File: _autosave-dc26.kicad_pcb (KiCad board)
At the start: 4 copper layers, 129.2 x 142.3 mm, 709 parts, among them J1 CONN_01X10, J2 CONN_01X10, J3 CONN_01X10, Y1 Crystal

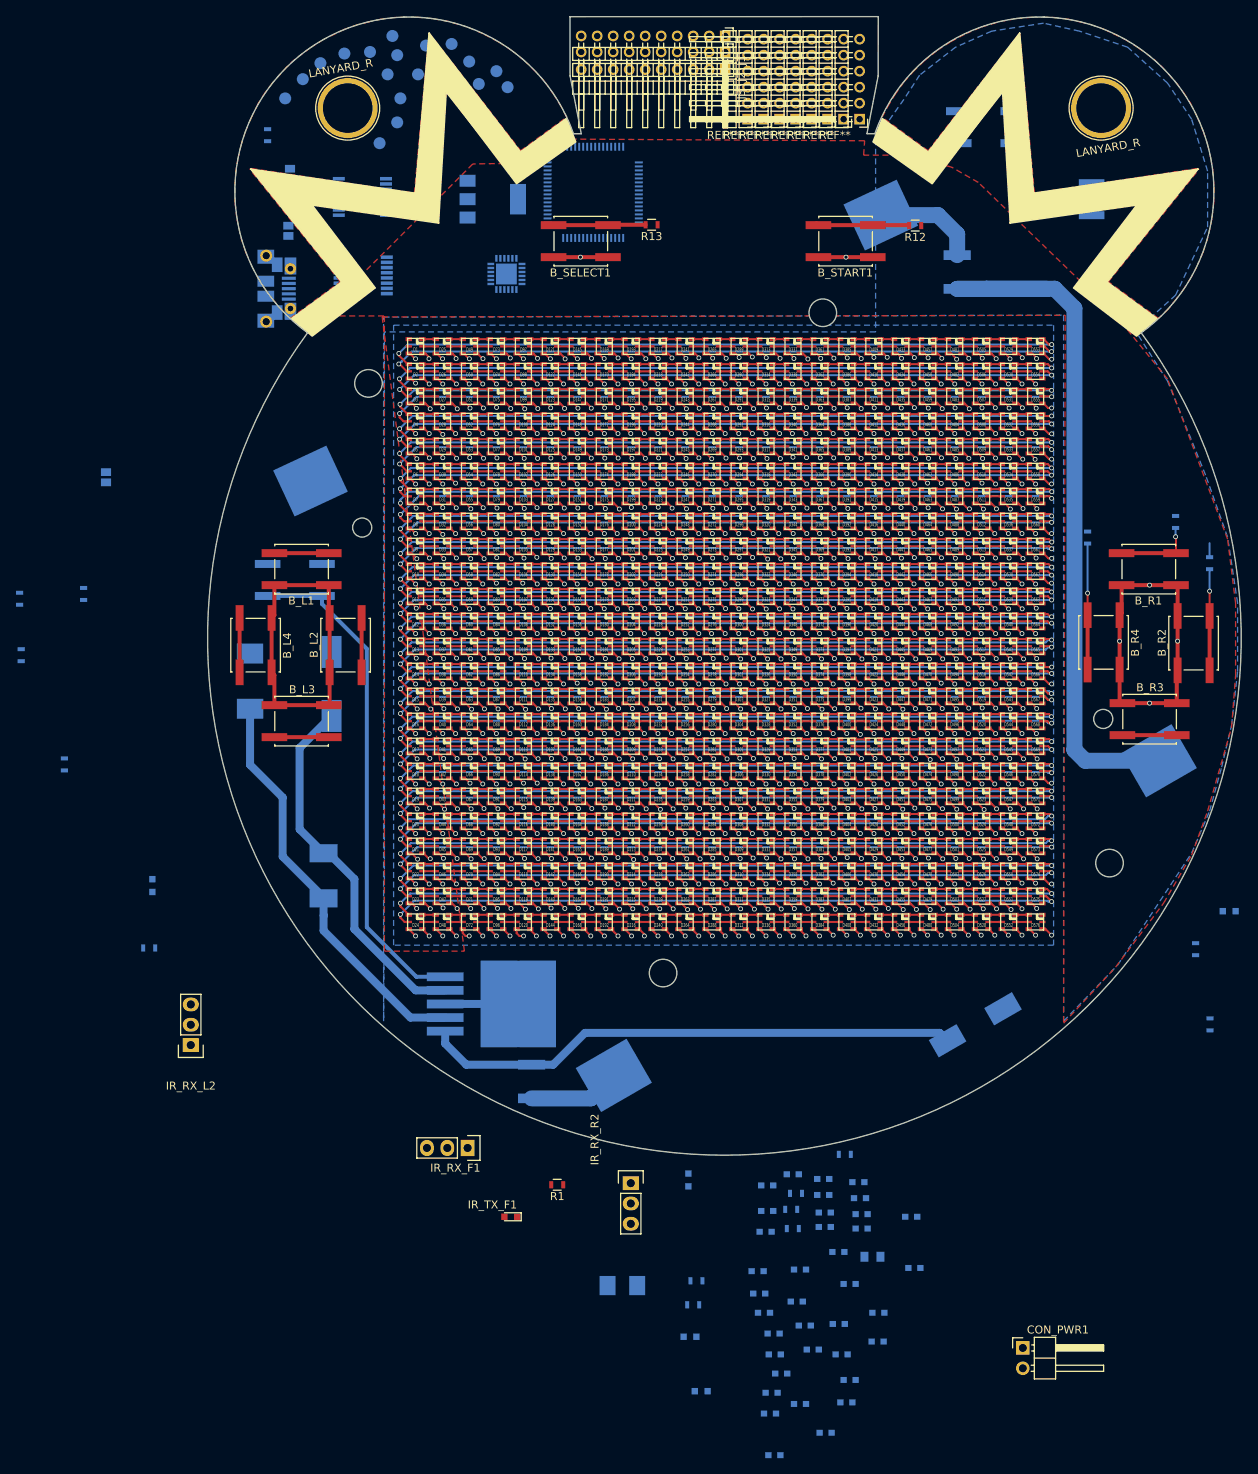
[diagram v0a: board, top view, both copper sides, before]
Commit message: zone movement + routing of all circuits
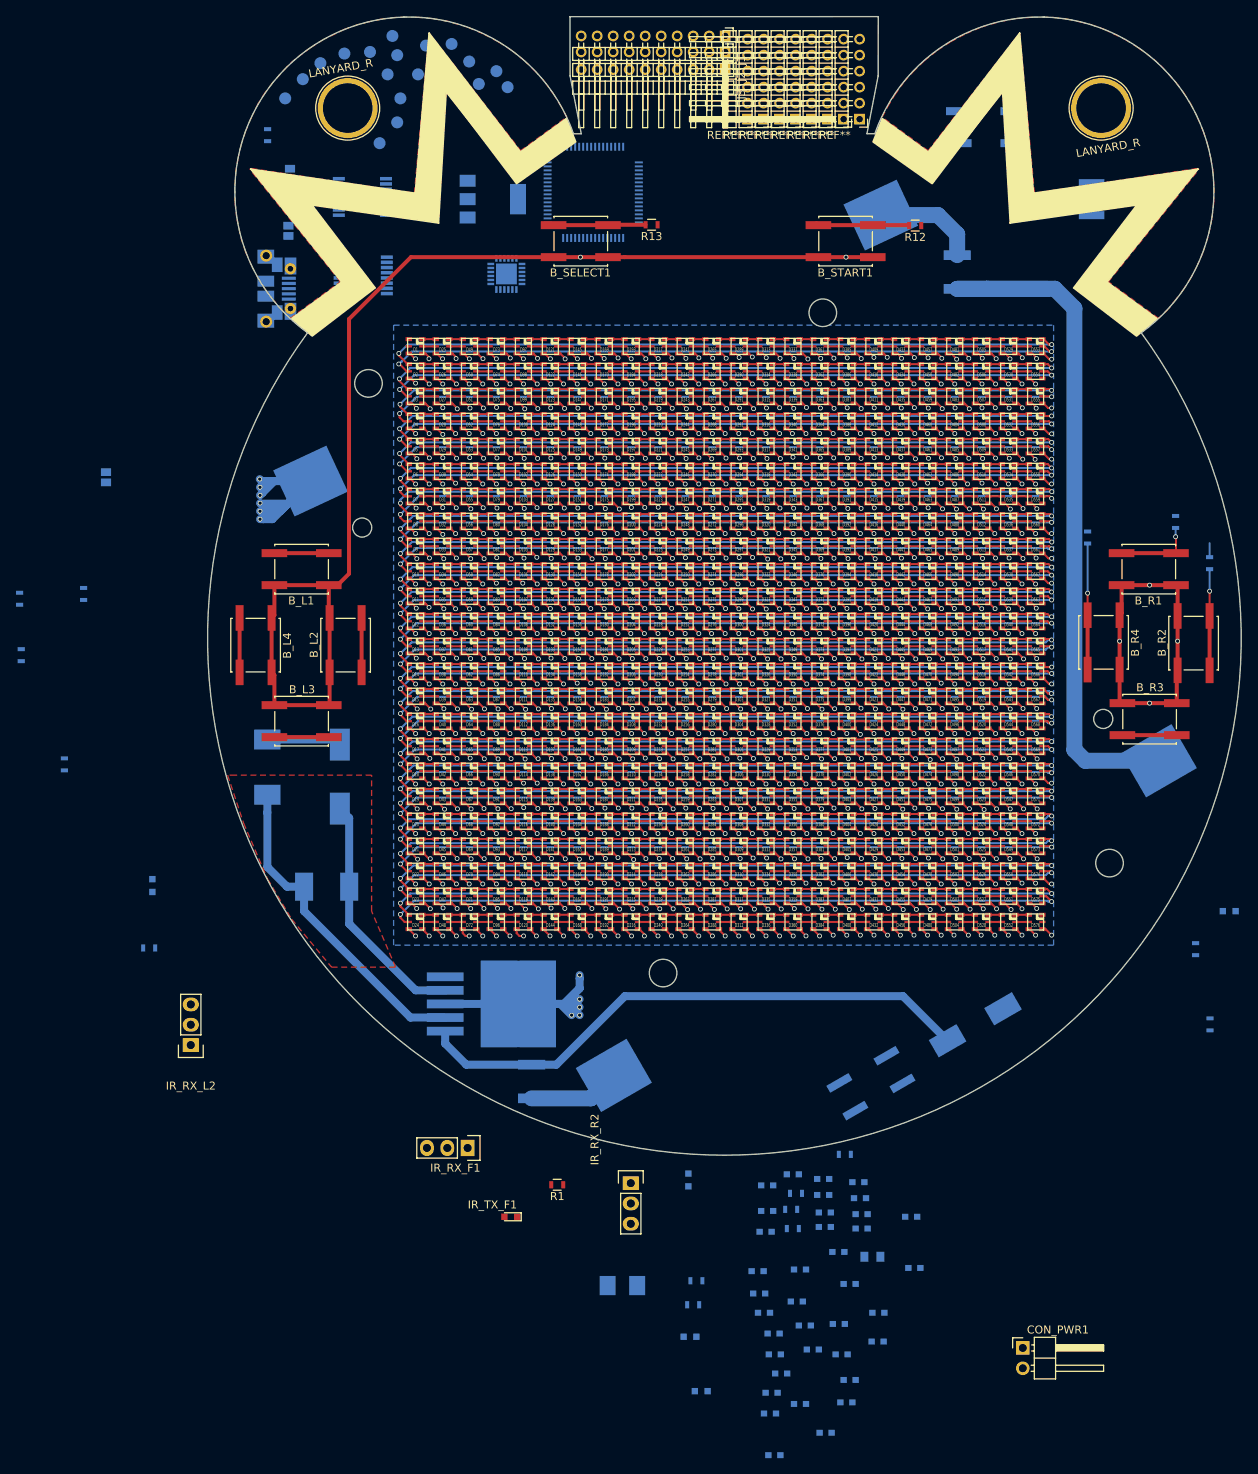
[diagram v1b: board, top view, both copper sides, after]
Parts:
- moved SW_PWRON1 95.6 mm to (193.4, 188.5), turned to 210 degrees
- moved BATT-BUCK-COUT1 11.6 mm to (127.0, 150.2)
- moved BATT-BUCK-SCHOTT1 11.0 mm to (118.0, 149.0)
- moved BATT-BUCK-INDUC1 1.41 mm to (125.4, 163.9), turned to 180 degrees
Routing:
- net GND: track 701.3 -> 798.4 mm, vias 576 -> 587
- net VCC: track 815.4 -> 889.8 mm
- net Net-(BATT-BUCK-PULLUP1-Pad1): track 62.9 -> 0.00 mm
- net Net-(BATT-BUCK-INDUC1-Pad2): track 51.2 -> 40.8 mm
- net BATT-BUCK-ENABLE: track 67.5 -> 71.3 mm
- removed copper zone on B.Cu, net GND
- removed copper zone on F.Cu, net GND

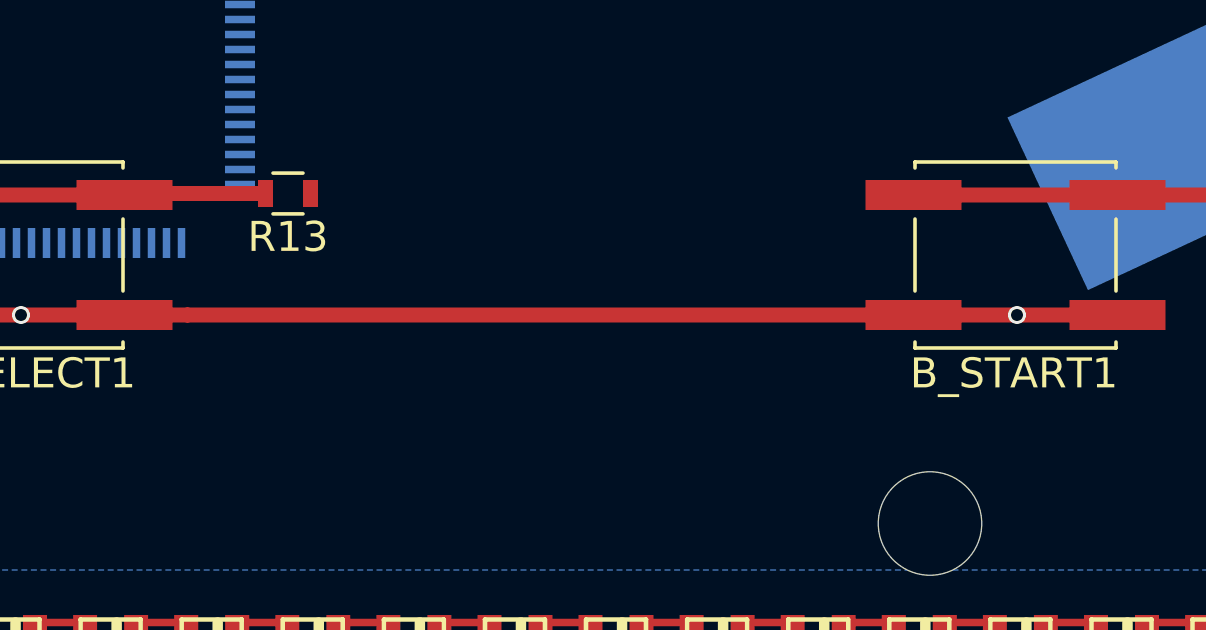
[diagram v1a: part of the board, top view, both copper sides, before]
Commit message: splitting led power out from 5v so that we can insert the mosfet
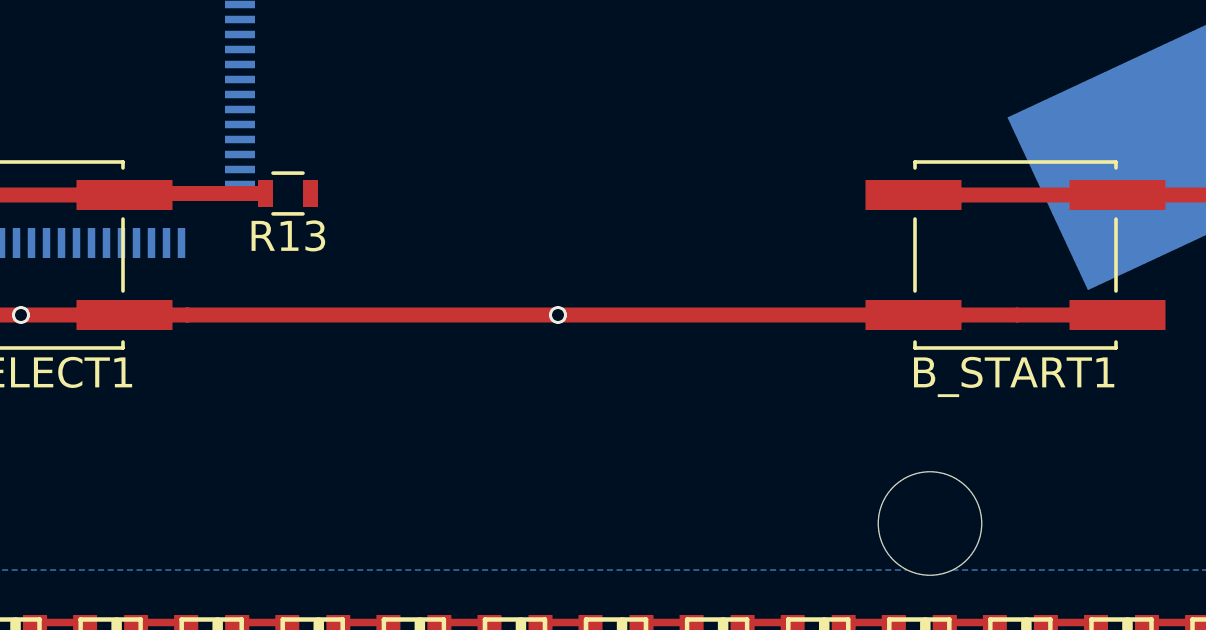
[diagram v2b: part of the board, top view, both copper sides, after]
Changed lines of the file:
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@@
     (thickness 1.6)
     (drawings 34)
-    (tracks 6102)
+    (tracks 6103)
     (zones 0)
     (modules 709)
@@
   (segment (start 172.715215 97.3) (end 173.139133 97.3) (width 0.25) (layer F.Cu) (net 1) (status 10))
   (segment (start 169.34565 97.3) (end 169.769568 97.3) (width 0.25) (layer F.Cu) (net 1) (status 10))
+  (segment (start 175 85.25) (end 186.85 85.25) (width 0.5) (layer F.Cu) (net 2))
+  (via (at 175 85.25) (size 0.6) (drill 0.4) (layers F.Cu B.Cu) (net 2))
+  (segment (start 162.65 85.25) (end 175 85.25) (width 0.5) (layer F.Cu) (net 2))
   (segment (start 160.55 85.25) (end 162.65 85.25) (width 0.5) (layer F.Cu) (net 2))
-  (segment (start 162.65 85.25) (end 186.85 85.25) (width 0.5) (layer F.Cu) (net 2))
   (segment (start 128.177265 92.982735) (end 135.91 85.25) (width 0.5) (layer F.Cu) (net 2))
   (segment (start 135.91 85.25) (end 153.75 85.25) (width 0.5) (layer F.Cu) (net 2))
@@
   (segment (start 190.3 85.25) (end 193.65 85.25) (width 0.5) (layer F.Cu) (net 2) (status 20))
   (segment (start 186.85 85.25) (end 190.3 85.25) (width 0.5) (layer F.Cu) (net 2) (status 10))
-  (via (at 190.3 85.25) (size 0.6) (drill 0.4) (layers F.Cu B.Cu) (net 2))
   (segment (start 157.1 85.25) (end 160.55 85.25) (width 0.5) (layer F.Cu) (net 2) (status 20))
   (segment (start 153.75 85.25) (end 157.1 85.25) (width 0.5) (layer F.Cu) (net 2) (status 10))
